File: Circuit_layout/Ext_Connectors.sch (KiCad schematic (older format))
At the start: 13 parts, among them CON1 AVR-JTAG-10, J1 Spare_Conns, J10 AIRs, J3 CAN, J4 Motor_Ctrl, J5 RJ12, P1 TSV, P2 HVPL, P3 IMD, P4 GLV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

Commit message: current sensor enable
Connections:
- net labels added: I_+5, I_RTN
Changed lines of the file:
@@
 ~RESET_AVR
 $Comp
-L +5V #PWR024
+L +5V #PWR027
 U 1 1 58A81530
 P 6100 6000
-F 0 "#PWR024" H 6100 5850 50  0001 C CNN
+F 0 "#PWR027" H 6100 5850 50  0001 C CNN
 F 1 "+5V" H 6100 6140 50  0000 C CNN
 F 2 "" H 6100 6000 50  0000 C CNN
@@
 +24V_RTN
 $Comp
-L +24V #PWR025
+L +24V #PWR028
 U 1 1 58AF1C5B
 P 1350 2600
-F 0 "#PWR025" H 1350 2450 50  0001 C CNN
+F 0 "#PWR028" H 1350 2450 50  0001 C CNN
 F 1 "+24V" H 1350 2740 50  0000 C CNN
 F 2 "" H 1350 2600 50  0000 C CNN
@@
 Drive_LED
 $Comp
-L +5V #PWR026
+L +5V #PWR029
 U 1 1 58B1052B
 P 7550 4000
-F 0 "#PWR026" H 7550 3850 50  0001 C CNN
+F 0 "#PWR029" H 7550 3850 50  0001 C CNN
 F 1 "+5V" H 7550 4140 50  0000 C CNN
 F 2 "" H 7550 4000 50  0000 C CNN
@@
 Throttle_RTN
 $Comp
-L GND #PWR027
+L GND #PWR030
 U 1 1 58B4A72F
 P 8650 3300
-F 0 "#PWR027" H 8650 3050 50  0001 C CNN
+F 0 "#PWR030" H 8650 3050 50  0001 C CNN
 F 1 "GND" H 8650 3150 50  0000 C CNN
 F 2 "" H 8650 3300 50  0000 C CNN
@@
 Text GLabel 8900 2250 0    60   Input ~ 0
 HVPL
-$Comp
-L +5V #PWR028
-U 1 1 58BB5596
-P 1700 1750
-F 0 "#PWR028" H 1700 1600 50  0001 C CNN
-F 1 "+5V" H 1700 1890 50  0000 C CNN
-F 2 "" H 1700 1750 50  0000 C CNN
-F 3 "" H 1700 1750 50  0000 C CNN
-	1    1700 1750
-	-1   0    0    1
-$EndComp
-$Comp
-L GND #PWR029
-U 1 1 58BB55DD
-P 1600 1900
-F 0 "#PWR029" H 1600 1650 50  0001 C CNN
-F 1 "GND" H 1600 1750 50  0000 C CNN
-F 2 "" H 1600 1900 50  0000 C CNN
-F 3 "" H 1600 1900 50  0000 C CNN
-	1    1600 1900
-	1    0    0    -1
-$EndComp
-Wire Wire Line
-	1700 1550 1700 1750
+Wire Wire Line
+	1700 1550 1700 1900
 Text GLabel 1500 1900 3    60   Input ~ 0
 A2_LV
@@
 CH_GND
 $Comp
-L GND #PWR030
+L GND #PWR031
 U 1 1 58B7A0E8
 P 7400 3800
-F 0 "#PWR030" H 7400 3550 50  0001 C CNN
+F 0 "#PWR031" H 7400 3550 50  0001 C CNN
 F 1 "GND" H 7400 3650 50  0000 C CNN
 F 2 "" H 7400 3800 50  0000 C CNN
@@
 CH_GND
 $Comp
-L GND #PWR031
+L GND #PWR032
 U 1 1 58B888D9
 P 1400 3250
-F 0 "#PWR031" H 1400 3000 50  0001 C CNN
+F 0 "#PWR032" H 1400 3000 50  0001 C CNN
 F 1 "GND" H 1400 3100 50  0000 C CNN
 F 2 "" H 1400 3250 50  0000 C CNN
@@
 	1350 2750 1350 2600
 $Comp
-L PWR_FLAG #FLG032
+L PWR_FLAG #FLG033
 U 1 1 58B89230
 P 1650 2600
-F 0 "#FLG032" H 1650 2695 50  0001 C CNN
+F 0 "#FLG033" H 1650 2695 50  0001 C CNN
 F 1 "PWR_FLAG" H 1650 2780 50  0000 C CNN
 F 2 "" H 1650 2600 50  0000 C CNN
@@
 Connection ~ 8800 2450
 $Comp
-L GND #PWR033
+L GND #PWR034
 U 1 1 58C3E939
 P 8800 2600
-F 0 "#PWR033" H 8800 2350 50  0001 C CNN
+F 0 "#PWR034" H 8800 2350 50  0001 C CNN
 F 1 "GND" H 8800 2450 50  0000 C CNN
 F 2 "" H 8800 2600 50  0000 C CNN
@@
 RTDS
 $Comp
-L GND #PWR034
+L GND #PWR035
 U 1 1 58D1CF0B
 P 5950 6500
-F 0 "#PWR034" H 5950 6250 50  0001 C CNN
+F 0 "#PWR035" H 5950 6250 50  0001 C CNN
 F 1 "GND" H 5950 6350 50  0000 C CNN
 F 2 "" H 5950 6500 50  0000 C CNN
@@
 	1    0    0    -1
 $EndComp
+Text GLabel 1600 1900 3    60   Input ~ 0
+I_RTN
+Text GLabel 1700 1900 3    60   Input ~ 0
+I_+5
 $EndSCHEMATC

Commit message: modifying hvpl
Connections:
- wire segments 68 -> 69
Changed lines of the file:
@@
 LIBS:xilinx
 LIBS:Zilog
-LIBS:pacman-main-cache
 LIBS:bss84
 LIBS:+10v
@@
 L GND #PWR031
 U 1 1 58B7A0E8
-P 7400 3800
-F 0 "#PWR031" H 7400 3550 50  0001 C CNN
-F 1 "GND" H 7400 3650 50  0000 C CNN
-F 2 "" H 7400 3800 50  0000 C CNN
-F 3 "" H 7400 3800 50  0000 C CNN
-	1    7400 3800
+P 7300 4000
+F 0 "#PWR031" H 7300 3750 50  0001 C CNN
+F 1 "GND" H 7300 3850 50  0000 C CNN
+F 2 "" H 7300 4000 50  0000 C CNN
+F 3 "" H 7300 4000 50  0000 C CNN
+	1    7300 4000
 	1    0    0    -1
 $EndComp
@@
 HVPL
 Wire Wire Line
-	7400 3800 9450 3800
+	7300 3800 9450 3800
 Text GLabel 1750 4800 2    60   Input ~ 0
 CANH
@@
 	8800 2450 9450 2450
 Wire Wire Line
-	8800 2350 8800 2600
+	8800 2350 8800 2650
 Connection ~ 8800 2450
 $Comp
 L GND #PWR034
 U 1 1 58C3E939
-P 8800 2600
-F 0 "#PWR034" H 8800 2350 50  0001 C CNN
-F 1 "GND" H 8800 2450 50  0000 C CNN
-F 2 "" H 8800 2600 50  0000 C CNN
-F 3 "" H 8800 2600 50  0000 C CNN
-	1    8800 2600
+P 8800 2650
+F 0 "#PWR034" H 8800 2400 50  0001 C CNN
+F 1 "GND" H 8800 2500 50  0000 C CNN
+F 2 "" H 8800 2650 50  0000 C CNN
+F 3 "" H 8800 2650 50  0000 C CNN
+	1    8800 2650
 	1    0    0    -1
 $EndComp
@@
 F 0 "P6" H 9650 1950 50  0000 C CNN
 F 1 "Pedals" V 9750 1450 50  0000 C CNN
-F 2 "" H 9650 1450 50  0000 C CNN
+F 2 "" H 9650 1450 50  0001 C CNN
 F 3 "" H 9650 1450 50  0000 C CNN
 	1    9650 1450
@@
 Text GLabel 1700 1900 3    60   Input ~ 0
 I_+5
+Wire Wire Line
+	7300 3800 7300 4000
 $EndSCHEMATC

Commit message: added footprint to DPDT switch, test points, DRC passes
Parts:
- added W?: +24V, Measurement_Points:Measurement_Point_Round-SMD-Pad_Big, symbol TEST_1P
- added W?: CH_GND, Measurement_Points:Measurement_Point_Square-SMD-Pad_Big, symbol TEST_1P
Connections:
- wire segments 69 -> 72
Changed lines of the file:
@@
 LIBS:xilinx
 LIBS:Zilog
+LIBS:pacman-main-cache
 LIBS:bss84
 LIBS:+10v
@@
 $EndComp
 Wire Wire Line
-	1200 3000 1400 3000
+	1200 3000 2100 3000
 Wire Wire Line
 	1400 3000 1400 3250
@@
 +24V
 Wire Wire Line
-	1100 2750 1650 2750
+	1100 2750 2050 2750
 Wire Wire Line
 	1350 2750 1350 2600
@@
 Wire Wire Line
 	7300 3800 7300 4000
+$Comp
+L PWR_FLAG #FLG036
+U 1 1 58D3F022
+P 1750 3250
+F 0 "#FLG036" H 1750 3345 50  0001 C CNN
+F 1 "PWR_FLAG" H 1750 3430 50  0000 C CNN
+F 2 "" H 1750 3250 50  0000 C CNN
+F 3 "" H 1750 3250 50  0000 C CNN
+	1    1750 3250
+	-1   0    0    1
+$EndComp
+Connection ~ 1400 3000
+$Comp
+L TEST_1P W?
+U 1 1 58D4655B
+P 2050 2600
+F 0 "W?" H 2050 2870 50  0000 C CNN
+F 1 "+24V" H 2050 2800 50  0000 C CNN
+F 2 "Measurement_Points:Measurement_Point_Round-SMD-Pad_Big" H 2250 2600 50  0001 C CNN
+F 3 "" H 2250 2600 50  0000 C CNN
+	1    2050 2600
+	1    0    0    -1
+$EndComp
+Wire Wire Line
+	2050 2750 2050 2600
+Connection ~ 1650 2750
+$Comp
+L TEST_1P W?
+U 1 1 58D46659
+P 2100 3200
+F 0 "W?" H 2100 3470 50  0000 C CNN
+F 1 "CH_GND" H 2100 3400 50  0000 C CNN
+F 2 "Measurement_Points:Measurement_Point_Square-SMD-Pad_Big" H 2300 3200 50  0001 C CNN
+F 3 "" H 2300 3200 50  0000 C CNN
+	1    2100 3200
+	-1   0    0    1
+$EndComp
+Wire Wire Line
+	1750 3000 1750 3250
+Wire Wire Line
+	2100 3000 2100 3200
+Connection ~ 1750 3000
 $EndSCHEMATC

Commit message: cleaned up footprints of more testpoints. ran DRC again, passed
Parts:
- gave numbers to parts that had none: 2
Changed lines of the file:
@@
 Connection ~ 1400 3000
 $Comp
-L TEST_1P W?
+L TEST_1P W16
 U 1 1 58D4655B
 P 2050 2600
-F 0 "W?" H 2050 2870 50  0000 C CNN
+F 0 "W16" H 2050 2870 50  0000 C CNN
 F 1 "+24V" H 2050 2800 50  0000 C CNN
 F 2 "Measurement_Points:Measurement_Point_Round-SMD-Pad_Big" H 2250 2600 50  0001 C CNN
@@
 Connection ~ 1650 2750
 $Comp
-L TEST_1P W?
+L TEST_1P W17
 U 1 1 58D46659
 P 2100 3200
-F 0 "W?" H 2100 3470 50  0000 C CNN
+F 0 "W17" H 2100 3470 50  0000 C CNN
 F 1 "CH_GND" H 2100 3400 50  0000 C CNN
 F 2 "Measurement_Points:Measurement_Point_Square-SMD-Pad_Big" H 2300 3200 50  0001 C CNN

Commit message: small changes
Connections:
- net labels removed: I_+5
- wire segments 72 -> 74
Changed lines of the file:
@@
 ~RESET_AVR
 $Comp
-L +5V #PWR027
+L +5V #PWR026
 U 1 1 58A81530
 P 6100 6000
-F 0 "#PWR027" H 6100 5850 50  0001 C CNN
+F 0 "#PWR026" H 6100 5850 50  0001 C CNN
 F 1 "+5V" H 6100 6140 50  0000 C CNN
 F 2 "" H 6100 6000 50  0000 C CNN
@@
 +24V_RTN
 $Comp
-L +24V #PWR028
+L +24V #PWR027
 U 1 1 58AF1C5B
 P 1350 2600
-F 0 "#PWR028" H 1350 2450 50  0001 C CNN
+F 0 "#PWR027" H 1350 2450 50  0001 C CNN
 F 1 "+24V" H 1350 2740 50  0000 C CNN
 F 2 "" H 1350 2600 50  0000 C CNN
@@
 Drive_LED
 $Comp
-L +5V #PWR029
+L +5V #PWR028
 U 1 1 58B1052B
 P 7550 4000
-F 0 "#PWR029" H 7550 3850 50  0001 C CNN
+F 0 "#PWR028" H 7550 3850 50  0001 C CNN
 F 1 "+5V" H 7550 4140 50  0000 C CNN
 F 2 "" H 7550 4000 50  0000 C CNN
@@
 Throttle_RTN
 $Comp
-L GND #PWR030
+L GND #PWR029
 U 1 1 58B4A72F
 P 8650 3300
-F 0 "#PWR030" H 8650 3050 50  0001 C CNN
+F 0 "#PWR029" H 8650 3050 50  0001 C CNN
 F 1 "GND" H 8650 3150 50  0000 C CNN
 F 2 "" H 8650 3300 50  0000 C CNN
@@
 CH_GND
 $Comp
-L GND #PWR031
+L GND #PWR030
 U 1 1 58B7A0E8
 P 7300 4000
-F 0 "#PWR031" H 7300 3750 50  0001 C CNN
+F 0 "#PWR030" H 7300 3750 50  0001 C CNN
 F 1 "GND" H 7300 3850 50  0000 C CNN
 F 2 "" H 7300 4000 50  0000 C CNN
@@
 CH_GND
 $Comp
-L GND #PWR032
+L GND #PWR031
 U 1 1 58B888D9
 P 1400 3250
-F 0 "#PWR032" H 1400 3000 50  0001 C CNN
+F 0 "#PWR031" H 1400 3000 50  0001 C CNN
 F 1 "GND" H 1400 3100 50  0000 C CNN
 F 2 "" H 1400 3250 50  0000 C CNN
@@
 	1350 2750 1350 2600
 $Comp
-L PWR_FLAG #FLG033
+L PWR_FLAG #FLG032
 U 1 1 58B89230
 P 1650 2600
-F 0 "#FLG033" H 1650 2695 50  0001 C CNN
+F 0 "#FLG032" H 1650 2695 50  0001 C CNN
 F 1 "PWR_FLAG" H 1650 2780 50  0000 C CNN
 F 2 "" H 1650 2600 50  0000 C CNN
@@
 Connection ~ 8800 2450
 $Comp
-L GND #PWR034
+L GND #PWR033
 U 1 1 58C3E939
 P 8800 2650
-F 0 "#PWR034" H 8800 2400 50  0001 C CNN
+F 0 "#PWR033" H 8800 2400 50  0001 C CNN
 F 1 "GND" H 8800 2500 50  0000 C CNN
 F 2 "" H 8800 2650 50  0000 C CNN
@@
 RTDS
 $Comp
-L GND #PWR035
+L GND #PWR034
 U 1 1 58D1CF0B
 P 5950 6500
-F 0 "#PWR035" H 5950 6250 50  0001 C CNN
+F 0 "#PWR034" H 5950 6250 50  0001 C CNN
 F 1 "GND" H 5950 6350 50  0000 C CNN
 F 2 "" H 5950 6500 50  0000 C CNN
@@
 Text GLabel 1600 1900 3    60   Input ~ 0
 I_RTN
-Text GLabel 1700 1900 3    60   Input ~ 0
-I_+5
 Wire Wire Line
 	7300 3800 7300 4000
 $Comp
-L PWR_FLAG #FLG036
+L PWR_FLAG #FLG035
 U 1 1 58D3F022
 P 1750 3250
-F 0 "#FLG036" H 1750 3345 50  0001 C CNN
+F 0 "#FLG035" H 1750 3345 50  0001 C CNN
 F 1 "PWR_FLAG" H 1750 3430 50  0000 C CNN
 F 2 "" H 1750 3250 50  0000 C CNN
@@
 	2100 3000 2100 3200
 Connection ~ 1750 3000
+$Comp
+L +5V #PWR?
+U 1 1 58D6E615
+P 2000 1800
+F 0 "#PWR?" H 2000 1650 50  0001 C CNN
+F 1 "+5V" H 2000 1940 50  0000 C CNN
+F 2 "" H 2000 1800 50  0000 C CNN
+F 3 "" H 2000 1800 50  0000 C CNN
+	1    2000 1800
+	1    0    0    -1
+$EndComp
+Wire Wire Line
+	1700 1900 2000 1900
+Wire Wire Line
+	2000 1900 2000 1800
 $EndSCHEMATC

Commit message: changed connectors
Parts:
- removed J10: AIRs, custom_footprints:TerminalBlock_Pheonix_MPT-5.08mm_2pol, symbol CONN_01X02
- removed J3: CAN, custom_footprints:TerminalBlock_Pheonix_MPT-5.08mm_2pol, symbol CONN_01X02
- removed P2: HVPL, custom_footprints:TerminalBlock_Pheonix_MPT-5.08mm_4pol, symbol CONN_01X04
- removed P3: IMD, custom_footprints:TerminalBlock_Pheonix_MPT-5.08mm_2pol, symbol CONN_01X02
- removed P4: GLV, custom_footprints:TerminalBlock_Pheonix_MPT-5.08mm_3pol, symbol CONN_01X03
- removed P5: Cockpit, custom_footprints:TerminalBlock_Pheonix_MPT-5.08mm_6pol, symbol CONN_01X06
- removed P6: Pedals, symbol CONN_01X09
- removed P7: RTDS, custom_footprints:TerminalBlock_Pheonix_MPT-5.08mm_2pol, symbol CONN_01X02
- added P?: CONN_02X07, Connect:IDC_Header_Straight_14pins, symbol CONN_02X07
- added P?: CONN_02X10, Connect:IDC_Header_Straight_20pins, symbol CONN_02X10
- J1: footprint custom_footprints:mkds_1,5-8 -> custom_footprints:Molex_8x1_2.54mm; Description (none) -> CONN HEADER 8POS .100 VERT 30AU; DigiKey P/N (none) -> WM4128-ND; Man P/N (none) -> 0705430112; Price (none) -> 1.88; URL (none) -> https://www.digikey.com/product-detail/en/molex-llc/0705430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
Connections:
- net labels added: HVPL_Cock, HVPL_Cock_RTN
- net labels removed: HV_Present_LED
- wire segments 74 -> 75
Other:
- note added: "HVPL"
- note added: "Pedals"
- note removed: "To Lights"
- note removed: "To Pedals"
- moved on the sheet: CON1, J1, J5, W16, W17

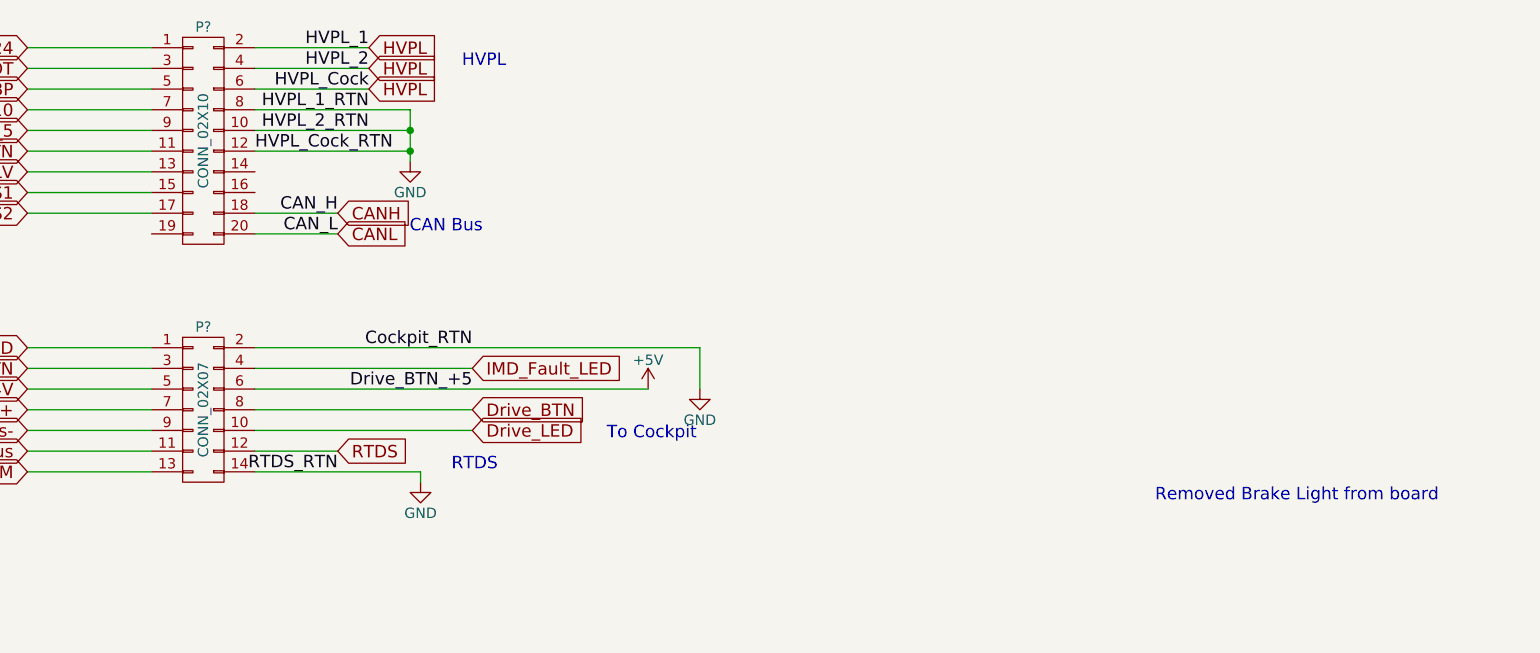
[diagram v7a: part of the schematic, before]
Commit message: made changes discussed in sch review w/ prof. added back +5 plane
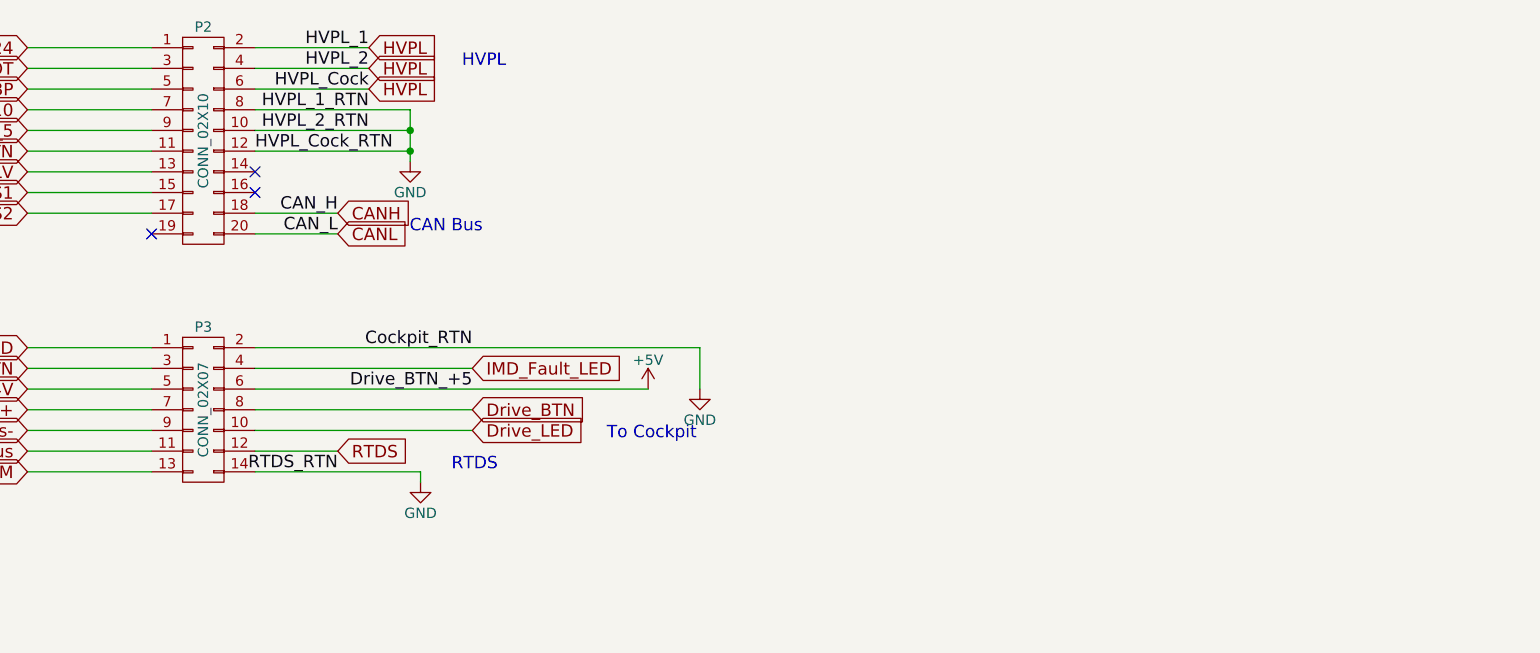
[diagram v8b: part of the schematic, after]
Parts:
- gave numbers to parts that had none: 2
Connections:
- no-connect marks 6 -> 9
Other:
- note removed: "Removed Brake Light from board"
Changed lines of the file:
@@
 ~RESET_AVR
 $Comp
-L +5V #PWR026
+L +5V #PWR022
 U 1 1 58A81530
 P 6800 4400
-F 0 "#PWR026" H 6800 4250 50  0001 C CNN
+F 0 "#PWR022" H 6800 4250 50  0001 C CNN
 F 1 "+5V" H 6800 4540 50  0000 C CNN
 F 2 "" H 6800 4400 50  0000 C CNN
@@
 +24V_RTN
 $Comp
-L +24V #PWR027
+L +24V #PWR023
 U 1 1 58AF1C5B
 P 2250 1250
-F 0 "#PWR027" H 2250 1100 50  0001 C CNN
+F 0 "#PWR023" H 2250 1100 50  0001 C CNN
 F 1 "+24V" H 2250 1390 50  0000 C CNN
 F 2 "" H 2250 1250 50  0000 C CNN
@@
 Drive_LED
 $Comp
-L +5V #PWR028
+L +5V #PWR024
 U 1 1 58B1052B
 P 8600 2700
-F 0 "#PWR028" H 8600 2550 50  0001 C CNN
+F 0 "#PWR024" H 8600 2550 50  0001 C CNN
 F 1 "+5V" H 8600 2840 50  0000 C CNN
 F 2 "" H 8600 2700 50  0000 C CNN
@@
 Throttle_RTN
 $Comp
-L GND #PWR029
+L GND #PWR025
 U 1 1 58B4A72F
 P 7500 3150
-F 0 "#PWR029" H 7500 2900 50  0001 C CNN
+F 0 "#PWR025" H 7500 2900 50  0001 C CNN
 F 1 "GND" H 7500 3000 50  0000 C CNN
 F 2 "" H 7500 3150 50  0000 C CNN
@@
 CH_GND
 $Comp
-L GND #PWR030
+L GND #PWR026
 U 1 1 58B7A0E8
 P 8850 2700
-F 0 "#PWR030" H 8850 2450 50  0001 C CNN
+F 0 "#PWR026" H 8850 2450 50  0001 C CNN
 F 1 "GND" H 8850 2550 50  0000 C CNN
 F 2 "" H 8850 2700 50  0000 C CNN
@@
 CH_GND
 $Comp
-L GND #PWR031
+L GND #PWR027
 U 1 1 58B888D9
 P 2300 1900
-F 0 "#PWR031" H 2300 1650 50  0001 C CNN
+F 0 "#PWR027" H 2300 1650 50  0001 C CNN
 F 1 "GND" H 2300 1750 50  0000 C CNN
 F 2 "" H 2300 1900 50  0000 C CNN
@@
 	2250 1400 2250 1250
 $Comp
-L PWR_FLAG #FLG032
+L PWR_FLAG #FLG028
 U 1 1 58B89230
 P 2550 1250
-F 0 "#FLG032" H 2550 1345 50  0001 C CNN
+F 0 "#FLG028" H 2550 1345 50  0001 C CNN
 F 1 "PWR_FLAG" H 2550 1430 50  0000 C CNN
 F 2 "" H 2550 1250 50  0000 C CNN
@@
 Connection ~ 7450 1450
 $Comp
-L GND #PWR033
+L GND #PWR029
 U 1 1 58C3E939
 P 7450 1600
-F 0 "#PWR033" H 7450 1350 50  0001 C CNN
+F 0 "#PWR029" H 7450 1350 50  0001 C CNN
 F 1 "GND" H 7450 1450 50  0000 C CNN
 F 2 "" H 7450 1600 50  0000 C CNN
@@
 Wire Wire Line
 	5600 1250 6200 1250
-Text Notes 11050 3250 0    60   ~ 0
-Removed Brake Light from board
 Wire Wire Line
 	7500 3100 7500 3150
@@
 RTDS
 $Comp
-L GND #PWR034
+L GND #PWR030
 U 1 1 58D1CF0B
 P 6650 4900
-F 0 "#PWR034" H 6650 4650 50  0001 C CNN
+F 0 "#PWR030" H 6650 4650 50  0001 C CNN
 F 1 "GND" H 6650 4750 50  0000 C CNN
 F 2 "" H 6650 4900 50  0000 C CNN
@@
 	8850 2500 8850 2700
 $Comp
-L PWR_FLAG #FLG035
+L PWR_FLAG #FLG031
 U 1 1 58D3F022
 P 2650 1900
-F 0 "#FLG035" H 2650 1995 50  0001 C CNN
+F 0 "#FLG031" H 2650 1995 50  0001 C CNN
 F 1 "PWR_FLAG" H 2650 2080 50  0000 C CNN
 F 2 "" H 2650 1900 50  0000 C CNN
@@
 Connection ~ 2650 1650
 $Comp
-L +5V #PWR?
+L +5V #PWR032
 U 1 1 58D6E615
 P 3100 3950
-F 0 "#PWR?" H 3100 3800 50  0001 C CNN
+F 0 "#PWR032" H 3100 3800 50  0001 C CNN
 F 1 "+5V" H 3100 4090 50  0000 C CNN
 F 2 "" H 3100 3950 50  0000 C CNN
@@
 	3100 4050 3100 3950
 $Comp
-L CONN_02X07 P?
+L CONN_02X07 P3
 U 1 1 58D5A394
 P 6450 2800
-F 0 "P?" H 6450 3200 50  0000 C CNN
+F 0 "P3" H 6450 3200 50  0000 C CNN
 F 1 "CONN_02X07" V 6450 2800 50  0000 C CNN
 F 2 "Connect:IDC_Header_Straight_14pins" H 6450 2350 50  0001 C CNN
@@
 $EndComp
 $Comp
-L CONN_02X10 P?
+L CONN_02X10 P2
 U 1 1 58D5A47F
 P 6450 1500
-F 0 "P?" H 6450 2050 50  0000 C CNN
+F 0 "P2" H 6450 2050 50  0000 C CNN
 F 1 "CONN_02X10" V 6450 1500 50  0000 C CNN
 F 2 "Connect:IDC_Header_Straight_20pins" H 6450 900 50  0001 C CNN
@@
 Text Notes 7700 1150 0    60   ~ 0
 HVPL
+NoConn ~ 6200 1950
+NoConn ~ 6700 1650
+NoConn ~ 6700 1750
 $EndSCHEMATC
